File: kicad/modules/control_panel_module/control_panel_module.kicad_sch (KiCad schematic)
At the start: 0 parts

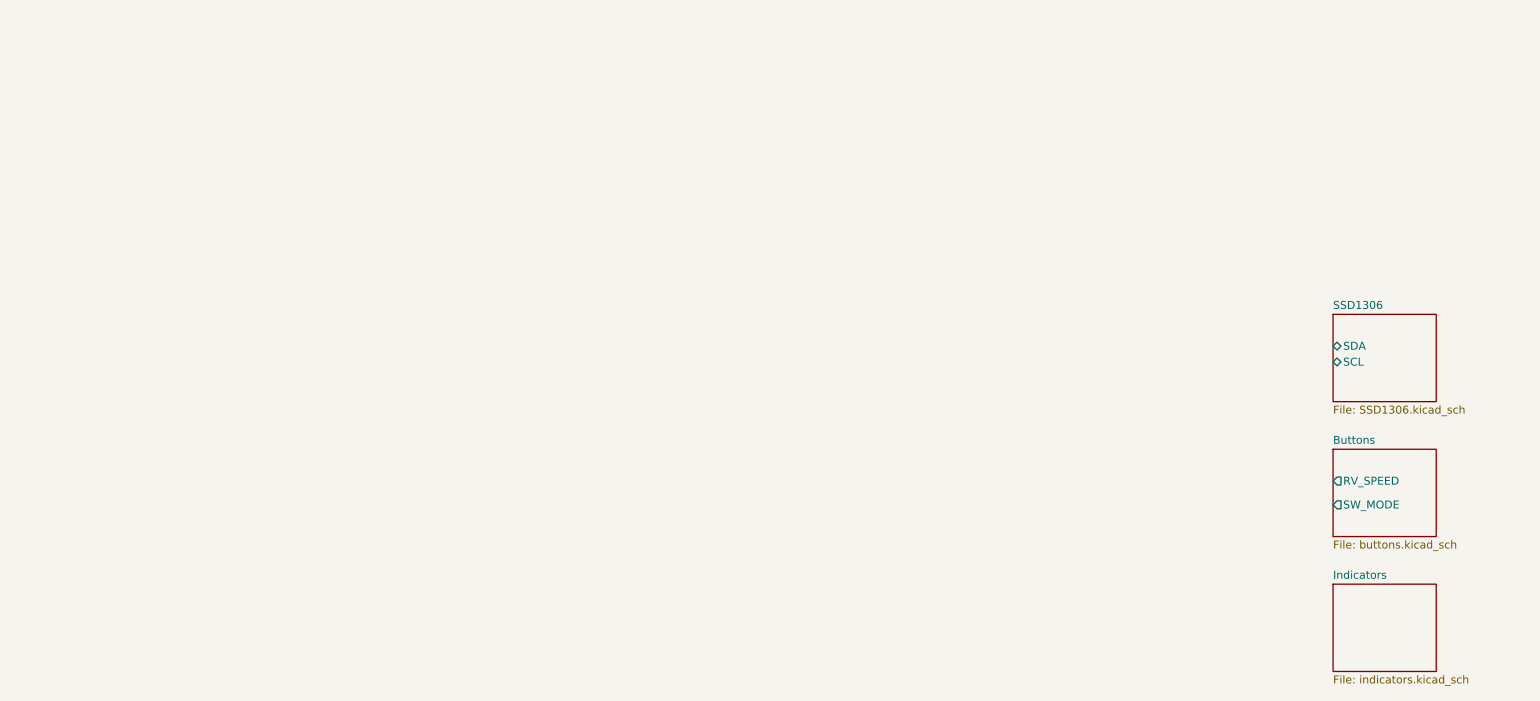
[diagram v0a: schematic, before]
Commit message: add control panel module
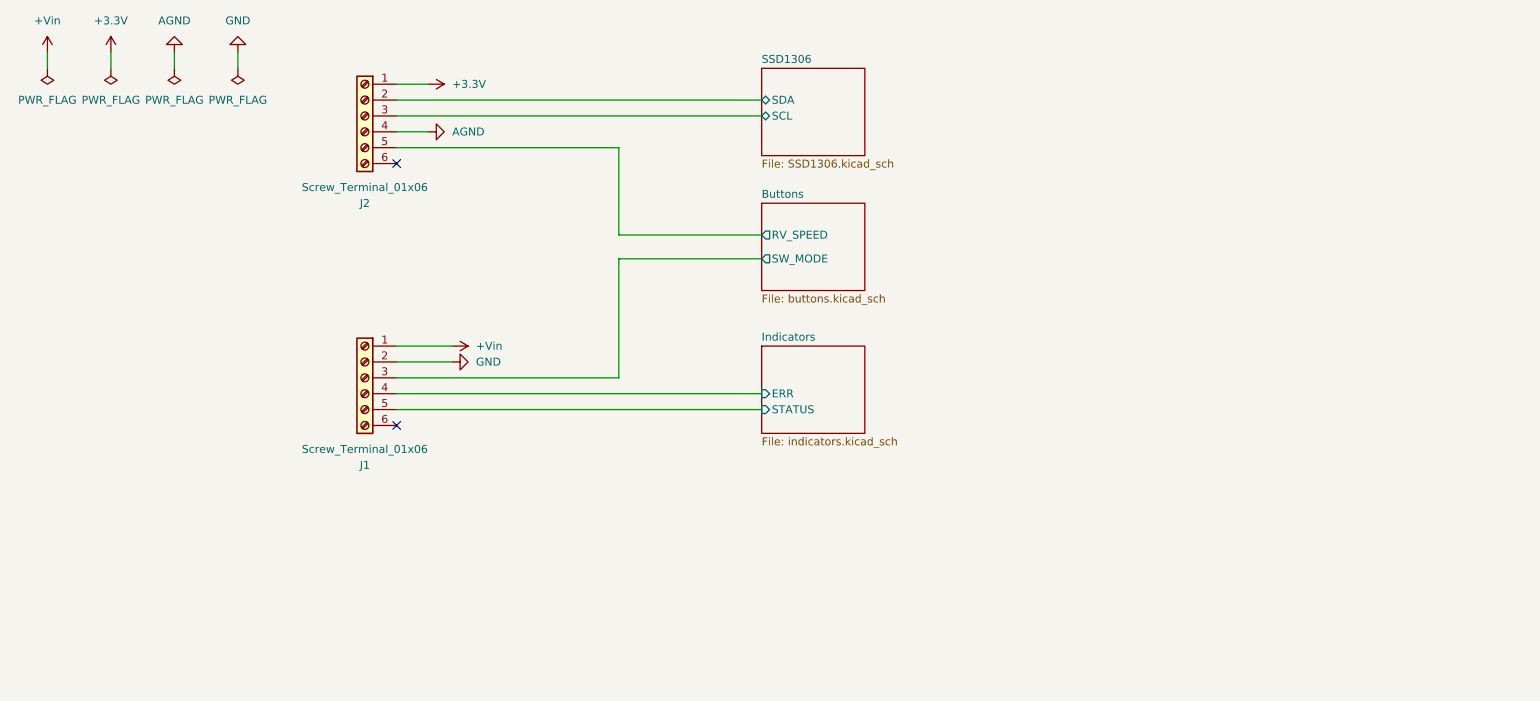
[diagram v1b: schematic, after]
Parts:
- added J1, J2: Screw_Terminal_01x06, Connector_PinHeader_2.54mm:PinHeader_1x06_P2.54mm_Vertical, symbol Connector:Screw_Terminal_01x06
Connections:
- net Buttons/RV_SPEED: now also J2.5 (Pin_5)
- net Buttons/SW_MODE: now also J1.3 (Pin_3)
- net SSD1306/SCL: now also J2.3 (Pin_3)
- net SSD1306/SDA: now also J2.2 (Pin_2)
- new net +3.3V: J2.1 (Pin_1)
- new net +Vin: J1.1 (Pin_1)
- new net AGND: J2.4 (Pin_4)
- new net GND: J1.2 (Pin_2)
- new net Indicators/ERR: J1.4 (Pin_4)
- new net Indicators/STATUS: J1.5 (Pin_5)
- no-connect marks 0 -> 2
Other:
- sheet Indicators ports: added ERR, STATUS; removed none
